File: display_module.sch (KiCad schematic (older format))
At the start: 0 parts

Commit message: Start of MIPI to HDMI converter schema
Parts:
- added J?: 46756-1001, antmicro-footprints:HDMI_Micro-D_Molex_46765-1x01, symbol antmicroUSBDVIHDMIConnectors:46756-1001
- added U?: LT9611, antmicro-footprints:LT9611, symbol antmicroInterfaceControllers:LT9611
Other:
- note added: "MIPI DSI to HDMI\n"
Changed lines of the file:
@@
 EELAYER 30 0
 EELAYER END
-$Descr A4 11693 8268
+$Descr A3 16535 11693
 encoding utf-8
 Sheet 5 6
@@
 Comment4 ""
 $EndDescr
+$Comp
+L antmicroInterfaceControllers:LT9611 U?
+U 1 1 61D8D19A
+P 2500 1600
+F 0 "U?" H 5244 437 50  0000 L CNN
+F 1 "LT9611" H 5244 346 50  0000 L CNN
+F 2 "antmicro-footprints:LT9611" H 2500 1600 50  0001 C CNN
+F 3 "" H 2500 1600 50  0001 C CNN
+F 4 "LT9611" H 5244 255 50  0000 L CNN "MPN"
+F 5 "LONTIUM" H 5244 164 50  0000 L CNN "Manufacturer"
+	1    2500 1600
+	1    0    0    -1
+$EndComp
+Text Notes 1150 800  0    50   ~ 0
+MIPI DSI to HDMI\n
+$Comp
+L antmicroUSBDVIHDMIConnectors:46756-1001 J?
+U 1 1 61D943B3
+P 9700 3100
+F 0 "J?" H 10130 3150 50  0000 L CNN
+F 1 "46756-1001" H 10130 3059 50  0000 L CNN
+F 2 "antmicro-footprints:HDMI_Micro-D_Molex_46765-1x01" H 9700 2000 50  0001 C CNN
+F 3 "https://www.molex.com/webdocs/datasheets/pdf/en-us/0467651001_IO_CONNECTORS.pdf" H 9700 3100 50  0001 C CNN
+F 4 "467651001" H 9700 1900 50  0001 C CNN "MPN"
+F 5 "Molex" H 9700 1800 50  0001 C CNN "Manufacturer"
+	1    9700 3100
+	1    0    0    -1
+$EndComp
 $EndSCHEMATC

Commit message: Added schema of Main and GNSS Antenna
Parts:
- U?: symbol antmicroInterfaceControllers:LT9611 -> sc606-baseboard-rescue:LT9611-antmicroInterfaceControllers
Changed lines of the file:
@@
 $EndDescr
 $Comp
-L antmicroInterfaceControllers:LT9611 U?
+L sc606-baseboard-rescue:LT9611-antmicroInterfaceControllers U?
 U 1 1 61D8D19A
 P 2500 1600

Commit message: Added annotations. Move to loclib
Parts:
- J4: renamed from J?; footprint antmicro-footprints:HDMI_Micro-D_Molex_46765-1x01 -> sc606-baseboard-footprints:HDMI_Micro-D_Molex_46765-1x01; symbol antmicroUSBDVIHDMIConnectors:46756-1001 -> sc606-baseboard:46756-1001
- U5: renamed from U?; footprint antmicro-footprints:LT9611 -> sc606-baseboard-footprints:LT9611; symbol sc606-baseboard-rescue:LT9611-antmicroInterfaceControllers -> sc606-baseboard:LT9611-antmicroInterfaceControllers
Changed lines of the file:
@@
 $EndDescr
 $Comp
-L sc606-baseboard-rescue:LT9611-antmicroInterfaceControllers U?
+L sc606-baseboard:LT9611-antmicroInterfaceControllers U5
 U 1 1 61D8D19A
 P 2500 1600
-F 0 "U?" H 5244 437 50  0000 L CNN
+F 0 "U5" H 5244 437 50  0000 L CNN
 F 1 "LT9611" H 5244 346 50  0000 L CNN
-F 2 "antmicro-footprints:LT9611" H 2500 1600 50  0001 C CNN
+F 2 "sc606-baseboard-footprints:LT9611" H 2500 1600 50  0001 C CNN
 F 3 "" H 2500 1600 50  0001 C CNN
 F 4 "LT9611" H 5244 255 50  0000 L CNN "MPN"
@@
 MIPI DSI to HDMI\n
 $Comp
-L antmicroUSBDVIHDMIConnectors:46756-1001 J?
+L sc606-baseboard:46756-1001 J4
 U 1 1 61D943B3
 P 9700 3100
-F 0 "J?" H 10130 3150 50  0000 L CNN
+F 0 "J4" H 10130 3150 50  0000 L CNN
 F 1 "46756-1001" H 10130 3059 50  0000 L CNN
-F 2 "antmicro-footprints:HDMI_Micro-D_Molex_46765-1x01" H 9700 2000 50  0001 C CNN
+F 2 "sc606-baseboard-footprints:HDMI_Micro-D_Molex_46765-1x01" H 9700 2000 50  0001 C CNN
 F 3 "https://www.molex.com/webdocs/datasheets/pdf/en-us/0467651001_IO_CONNECTORS.pdf" H 9700 3100 50  0001 C CNN
 F 4 "467651001" H 9700 1900 50  0001 C CNN "MPN"

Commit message: Block diagram update
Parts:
- J4: footprint sc606-baseboard-footprints:HDMI_Micro-D_Molex_46765-1x01 -> antmicro-footprints:HDMI_Micro-D_Molex_46765-1x01; symbol sc606-baseboard:46756-1001 -> antmicroUSBDVIHDMIConnectors:46756-1001
- U5: footprint sc606-baseboard-footprints:LT9611 -> antmicro-footprints:LT9611; symbol sc606-baseboard:LT9611-antmicroInterfaceControllers -> sc606-baseboard-rescue:LT9611-antmicroInterfaceControllers
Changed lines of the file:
@@
 $EndDescr
 $Comp
-L sc606-baseboard:LT9611-antmicroInterfaceControllers U5
+L sc606-baseboard-rescue:LT9611-antmicroInterfaceControllers U5
 U 1 1 61D8D19A
 P 2500 1600
 F 0 "U5" H 5244 437 50  0000 L CNN
 F 1 "LT9611" H 5244 346 50  0000 L CNN
-F 2 "sc606-baseboard-footprints:LT9611" H 2500 1600 50  0001 C CNN
+F 2 "antmicro-footprints:LT9611" H 2500 1600 50  0001 C CNN
 F 3 "" H 2500 1600 50  0001 C CNN
 F 4 "LT9611" H 5244 255 50  0000 L CNN "MPN"
@@
 MIPI DSI to HDMI\n
 $Comp
-L sc606-baseboard:46756-1001 J4
+L antmicroUSBDVIHDMIConnectors:46756-1001 J4
 U 1 1 61D943B3
 P 9700 3100
 F 0 "J4" H 10130 3150 50  0000 L CNN
 F 1 "46756-1001" H 10130 3059 50  0000 L CNN
-F 2 "sc606-baseboard-footprints:HDMI_Micro-D_Molex_46765-1x01" H 9700 2000 50  0001 C CNN
+F 2 "antmicro-footprints:HDMI_Micro-D_Molex_46765-1x01" H 9700 2000 50  0001 C CNN
 F 3 "https://www.molex.com/webdocs/datasheets/pdf/en-us/0467651001_IO_CONNECTORS.pdf" H 9700 3100 50  0001 C CNN
 F 4 "467651001" H 9700 1900 50  0001 C CNN "MPN"

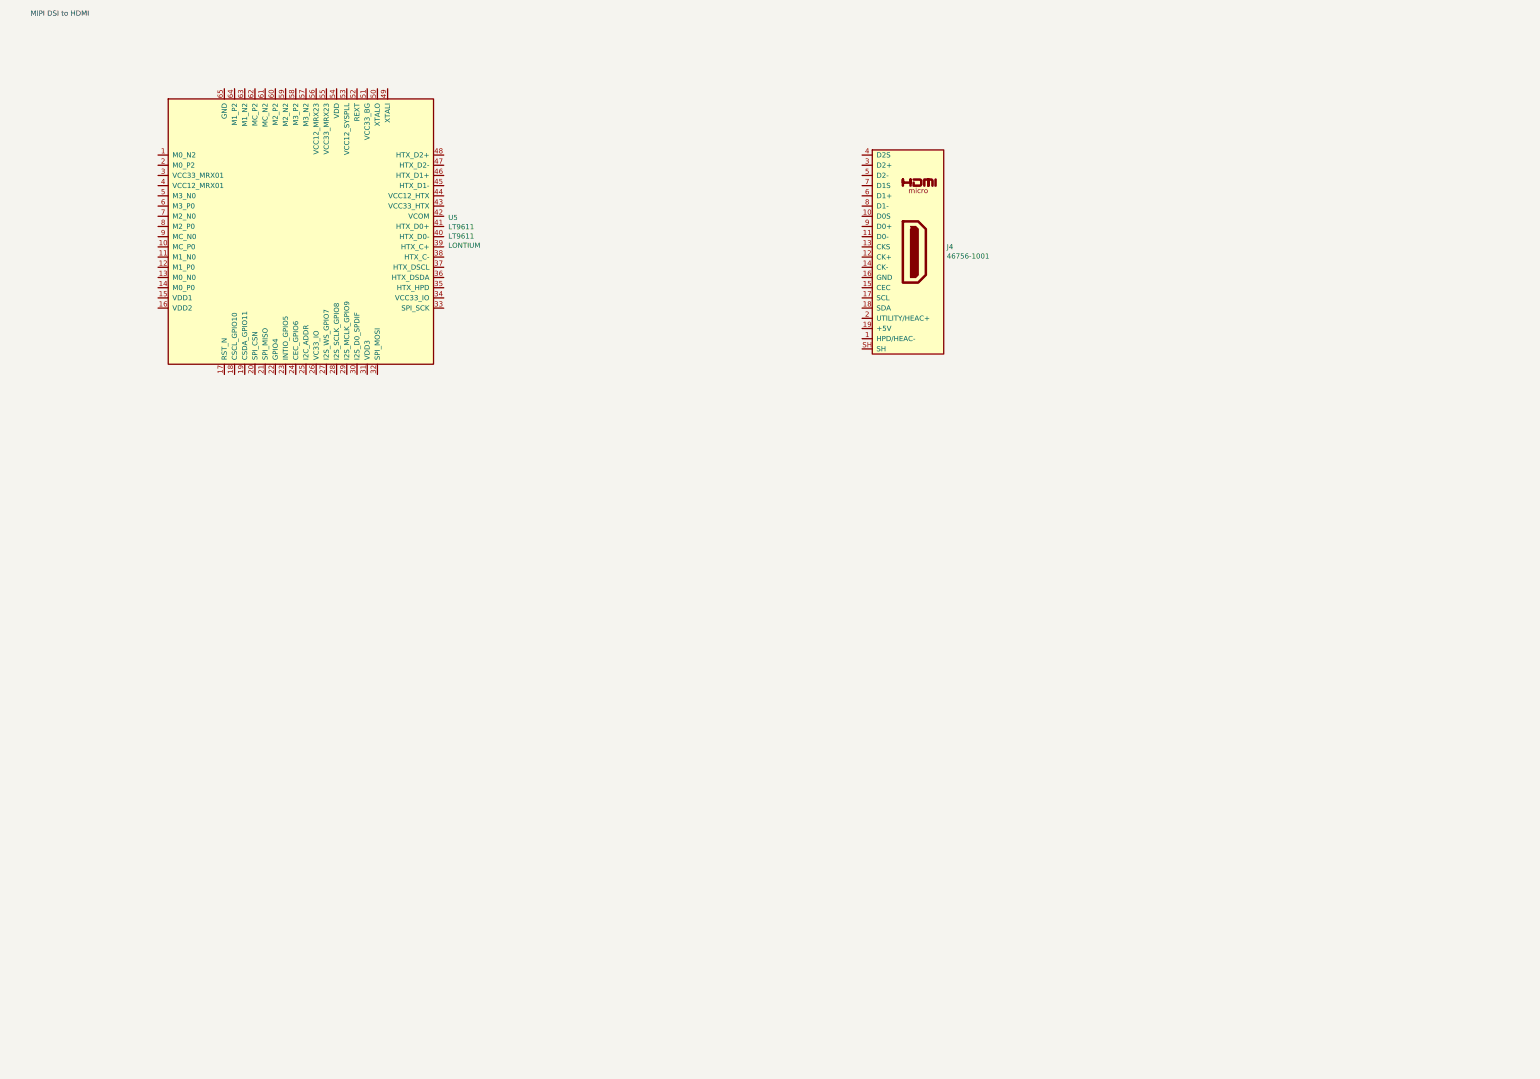
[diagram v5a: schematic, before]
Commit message: Added connectors to LCD displays
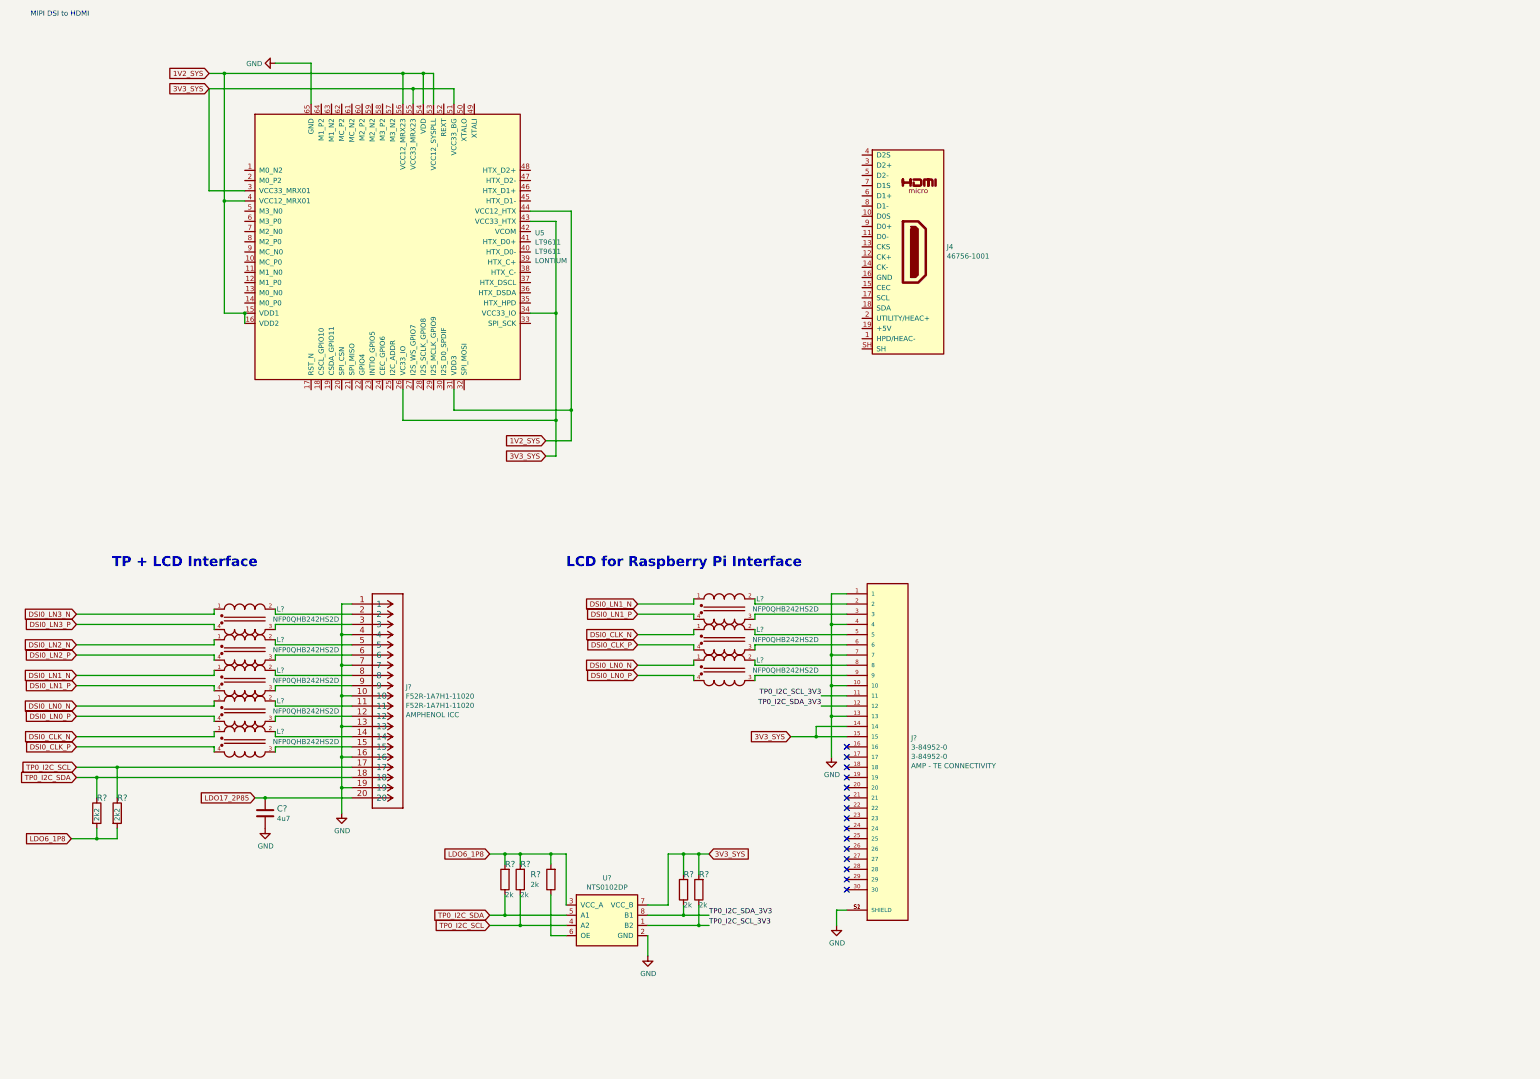
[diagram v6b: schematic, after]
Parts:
- added C?: C_4u7_0402, antmicro-footprints:0402-cap, symbol antmicroCapacitors0402:C_4u7_0402
- added J?: F52R-1A7H1-11020, antmicro-footprints:F52R-1A7H1-11020, symbol antmicroFCCConnectors:F52R-1A7H1-11020
- added J?: 3-84952-0, symbol antmicroFCCConnectors:3-84952-0
- added L? (x8): NFP0QHB242HS2D, antmicro-footprints:FIL_NFP0QHB242HS2D, symbol antmicroFixedInductors:NFP0QHB242HS2D
- added R? (x2): R_2k2_0402, antmicro-footprints:0402-res, symbol antmicroResistors0402:R_2k2_0402
- added R? (x5): R_2k_0402, antmicro-footprints:0402-res, symbol antmicroResistors0402:R_2k_0402
- added U?: NTS0102DP, antmicro-footprints:TSSOP-8_W3mm, symbol antmicroLogicTranslatorsLevelShifters:NTS0102DP
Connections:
- net 1V2_SYS: now reaches U5.15 (VDD1)
- net 1V2_SYS: now also U5.16 (VDD2), U5.31 (VDD3), U5.4 (VCC12_MRX01), U5.44 (VCC12_HTX), U5.53 (VCC12_SYSPLL), U5.54 (VDD), U5.56 (VCC12_MRX23)
- net 3V3_SYS: now reaches U5.26 (VC33_IO)
- net 3V3_SYS: now also U5.3 (VCC33_MRX01), U5.34 (VCC33_IO), U5.43 (VCC33_HTX), U5.51 (VCC33_BG), U5.55 (VCC33_MRX23), J?.14, J?.15, R?.2, R?.2, U?.7 (VCC_B)
- net GND: now reaches U5.65 (GND)
- net GND: now also C?.2, J?.1, J?.1, J?.10, J?.10, J?.13, J?.13, J?.16, J?.19, J?.4, J?.4, J?.7, J?.7, J?.S1 (SHIELD), J?.S2 (SHIELD), U?.2 (GND)
- new net: J?.11, L?.2
- new net: J?.12, L?.3
- new net: J?.14, L?.2
- new net: J?.15, L?.3
- new net: J?.2, L?.2 (x2)
- new net: J?.3, L?.3 (x2)
- new net: J?.5, L?.2 (x2)
- new net: J?.6, L?.3 (x2)
- new net: J?.8, L?.2 (x2)
- new net: J?.9, L?.3 (x2)
- new net: R?.1, U?.6 (OE)
- new net DSI0_CLK_N: L?.1, L?.1
- new net DSI0_CLK_P: L?.4, L?.4
- new net DSI0_LN0_N: L?.1, L?.1
- new net DSI0_LN0_P: L?.4, L?.4
- new net DSI0_LN1_N: L?.1, L?.1
- new net DSI0_LN1_P: L?.4, L?.4
- new net DSI0_LN2_N: L?.1
- new net DSI0_LN2_P: L?.4
- new net DSI0_LN3_N: L?.1
- new net DSI0_LN3_P: L?.4
- new net LDO17_2P85: C?.1, J?.20
- new net LDO6_1P8: R?.2, R?.2, R?.2, R?.2, R?.2, U?.3 (VCC_A)
- new net TP0_I2C_SCL: J?.17, R?.1, R?.1, U?.4 (A2)
- new net TP0_I2C_SCL_3V3: J?.11, R?.1, U?.1 (B2)
- new net TP0_I2C_SDA: J?.18, R?.1, R?.1, U?.5 (A1)
- new net TP0_I2C_SDA_3V3: J?.12, R?.1, U?.8 (B1)
- no-connect marks 0 -> 15
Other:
- note added: "LCD for Raspberry Pi Interface"
- note added: "TP + LCD Interface"
- moved on the sheet: U5

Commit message: Added keypads and no flag connections to unused pins
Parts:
- C?: footprint antmicro-footprints:0402-cap -> sc606-baseboard-footprints:0402-cap; symbol antmicroCapacitors0402:C_4u7_0402 -> sc606-baseboard:C_4u7_0402
- J4: footprint antmicro-footprints:HDMI_Micro-D_Molex_46765-1x01 -> sc606-baseboard-footprints:HDMI_Micro-D_Molex_46765-1x01; symbol antmicroUSBDVIHDMIConnectors:46756-1001 -> sc606-baseboard:46756-1001
- J?: footprint antmicro-footprints:F52R-1A7H1-11020 -> sc606-baseboard-footprints:F52R-1A7H1-11020; symbol antmicroFCCConnectors:F52R-1A7H1-11020 -> sc606-baseboard:F52R-1A7H1-11020
- J?: symbol antmicroFCCConnectors:3-84952-0 -> sc606-baseboard:3-84952-0
- L? (x8): footprint antmicro-footprints:FIL_NFP0QHB242HS2D -> sc606-baseboard-footprints:FIL_NFP0QHB242HS2D; symbol antmicroFixedInductors:NFP0QHB242HS2D -> sc606-baseboard:NFP0QHB242HS2D
- R? (x2): footprint antmicro-footprints:0402-res -> sc606-baseboard-footprints:0402-res; symbol antmicroResistors0402:R_2k2_0402 -> sc606-baseboard:R_2k2_0402
- R? (x5): footprint antmicro-footprints:0402-res -> sc606-baseboard-footprints:0402-res; symbol antmicroResistors0402:R_2k_0402 -> sc606-baseboard:R_2k_0402
- U5: footprint antmicro-footprints:LT9611 -> sc606-baseboard-footprints:LT9611; symbol sc606-baseboard-rescue:LT9611-antmicroInterfaceControllers -> sc606-baseboard:LT9611-antmicroInterfaceControllers
- U?: footprint antmicro-footprints:TSSOP-8_W3mm -> sc606-baseboard-footprints:TSSOP-8_W3mm; symbol antmicroLogicTranslatorsLevelShifters:NTS0102DP -> sc606-baseboard:NTS0102DP
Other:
- moved on the sheet: J4

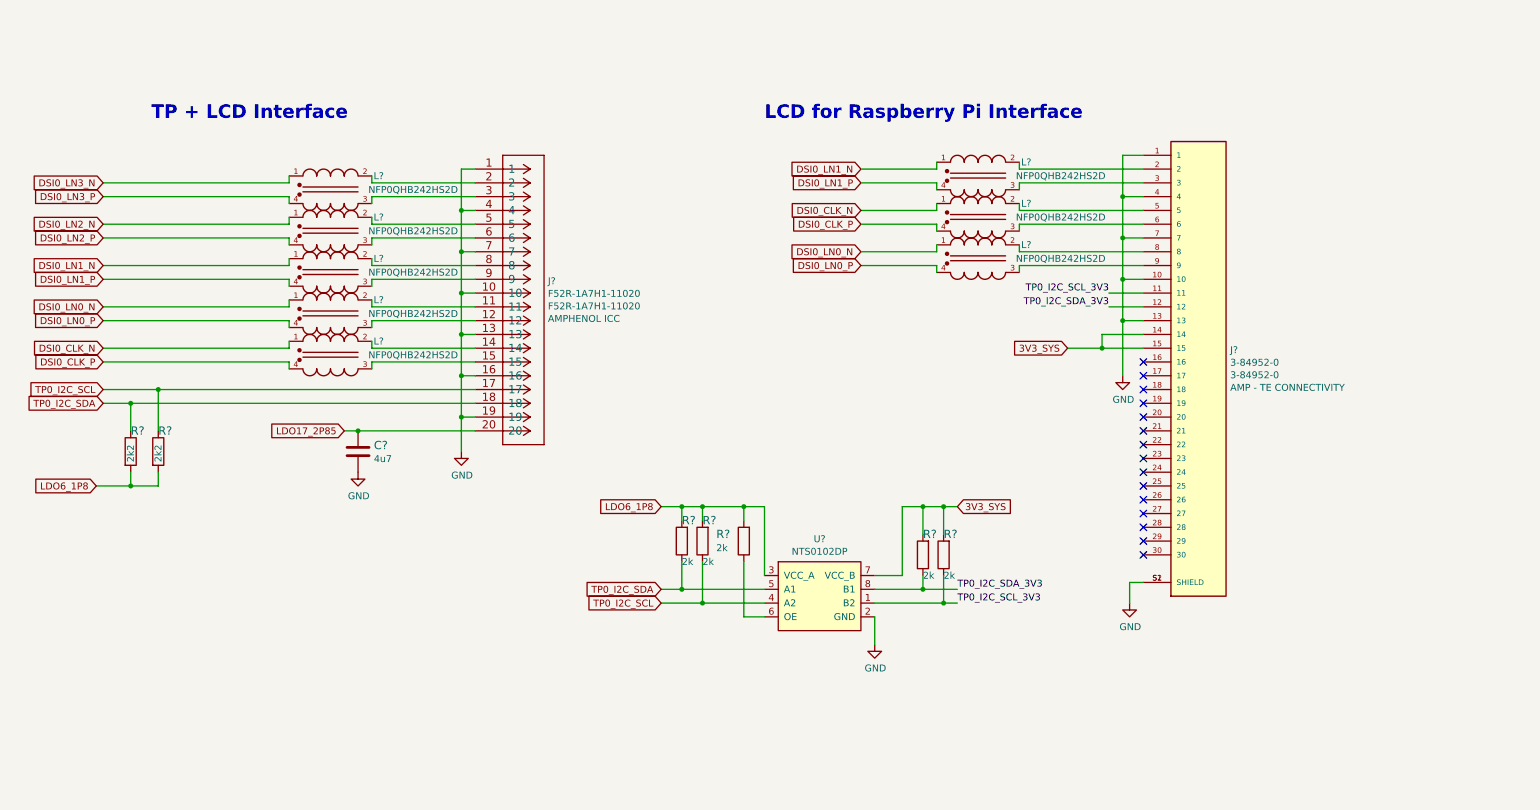
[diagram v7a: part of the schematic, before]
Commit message: Change DC/DC converters to match project SA800u
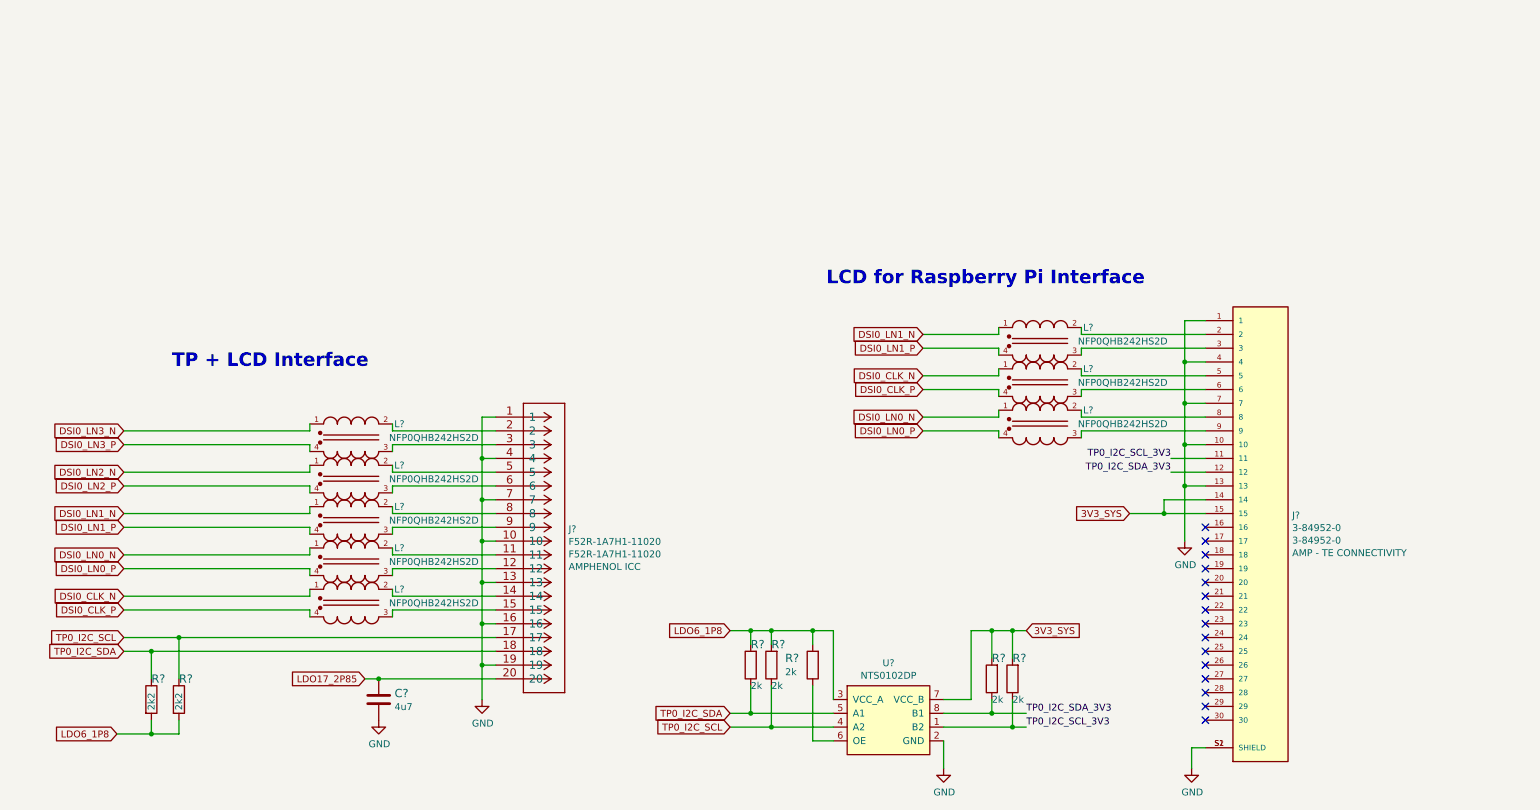
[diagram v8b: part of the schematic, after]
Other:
- moved on the sheet: C?, J?, L?, R?, U?
